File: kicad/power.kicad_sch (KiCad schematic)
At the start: 27 parts, among them U3 MIMXRT1171DVMAB, Y3 24MHz, Y4 32.768kHz

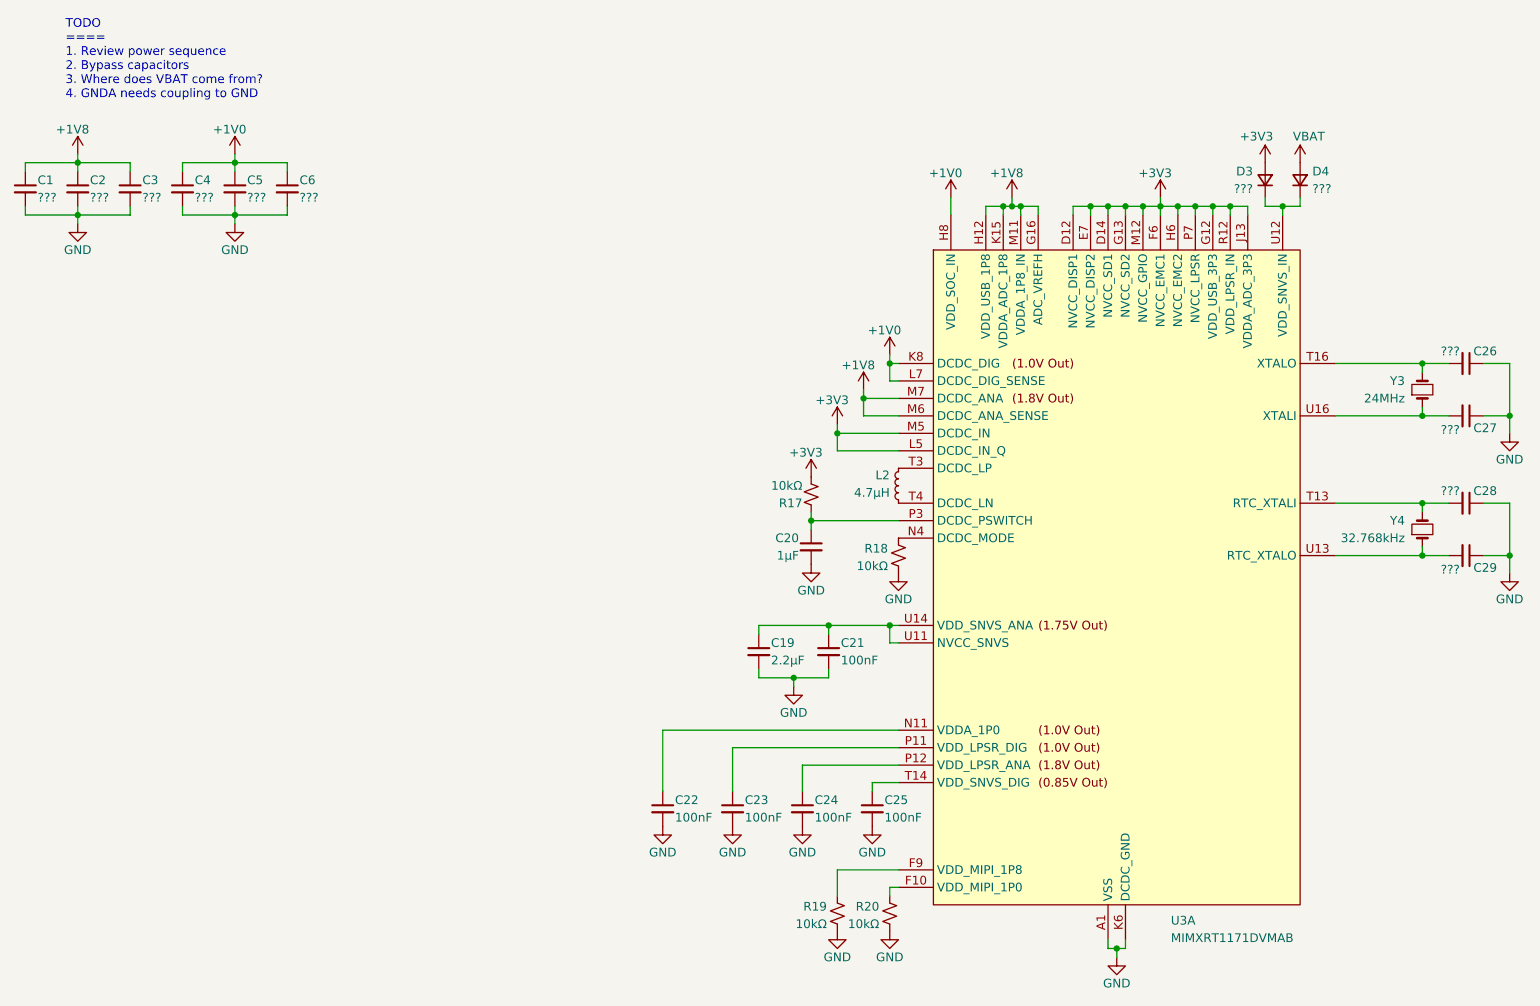
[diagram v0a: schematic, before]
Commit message: reworked design to use 1.8V logic
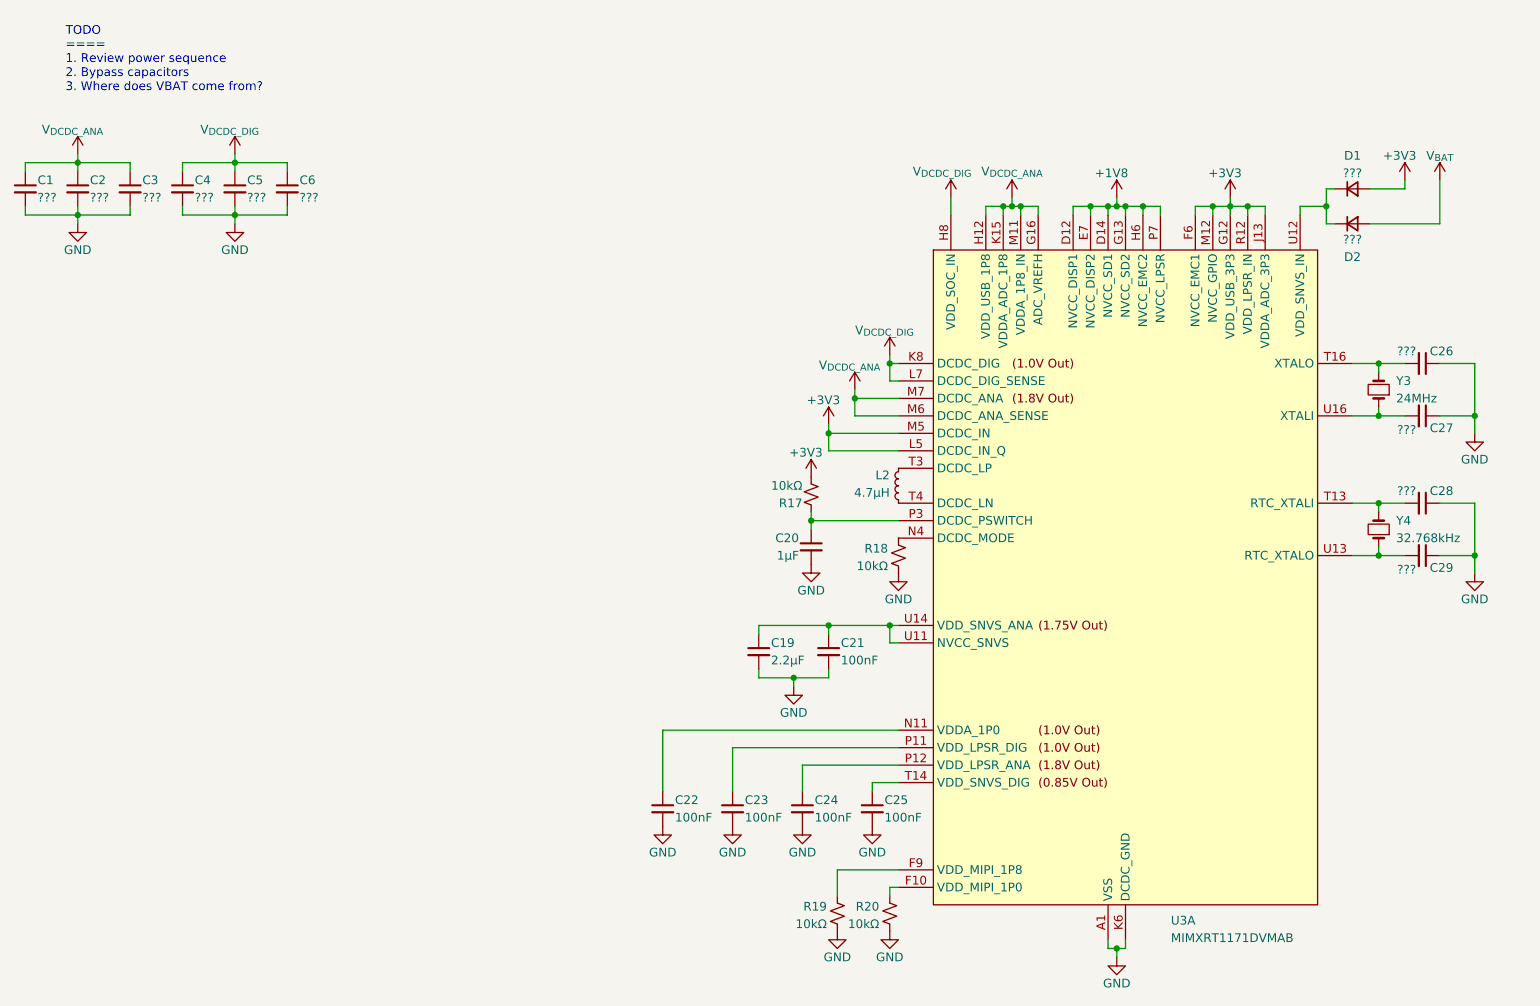
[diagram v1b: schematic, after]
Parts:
- removed D3, D4: ???, symbol Device:D_Small
- added D1, D2: ???, symbol Device:D_Small
- U3: footprint (none) -> Package_BGA:MAPBGA-289_14x14mm_Layout17x17_P0.8mm
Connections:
- net +1V8: now also U3.D12 (NVCC_DISP1), U3.D14 (NVCC_SD1), U3.E7 (NVCC_DISP2), U3.G13 (NVCC_SD2), U3.H6 (NVCC_EMC2), U3.J6 (NVCC_EMC2), U3.P7 (NVCC_LPSR); no longer C1.1, C2.1, C3.1, U3.G16 (ADC_VREFH), U3.H12 (VDD_USB_1P8), U3.K15 (VDDA_ADC_1P8), U3.M11 (VDDA_1P8_IN), U3.M6 (DCDC_ANA_SENSE), U3.M7 (DCDC_ANA), U3.M8 (DCDC_ANA)
- net +3V3: now also D1.2 (A); no longer U3.D12 (NVCC_DISP1), U3.D14 (NVCC_SD1), U3.E7 (NVCC_DISP2), U3.G13 (NVCC_SD2), U3.H6 (NVCC_EMC2), U3.J6 (NVCC_EMC2), U3.P7 (NVCC_LPSR)
- net at U3.U12 (VDD_SNVS_IN): now also D1.1 (K), D2.1 (K)
- net +1V0 renamed V_{DCDC_DIG}
- new net V_{BAT}: D2.2 (A)
- new net V_{DCDC_ANA}: C1.1, C2.1, C3.1, U3.G16 (ADC_VREFH), U3.H12 (VDD_USB_1P8), U3.K15 (VDDA_ADC_1P8), U3.M11 (VDDA_1P8_IN), U3.M6 (DCDC_ANA_SENSE), U3.M7 (DCDC_ANA), U3.M8 (DCDC_ANA)
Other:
- note added: "TODO ==== 1. Review power sequence 2. Bypass capacitors 3. Where does VBAT come from?"
- note removed: "TODO ==== 1. Review power sequence 2. Bypass capacitors 3. Where does VBAT come from? 4. GNDA needs coupling to GND"
- moved on the sheet: U3A

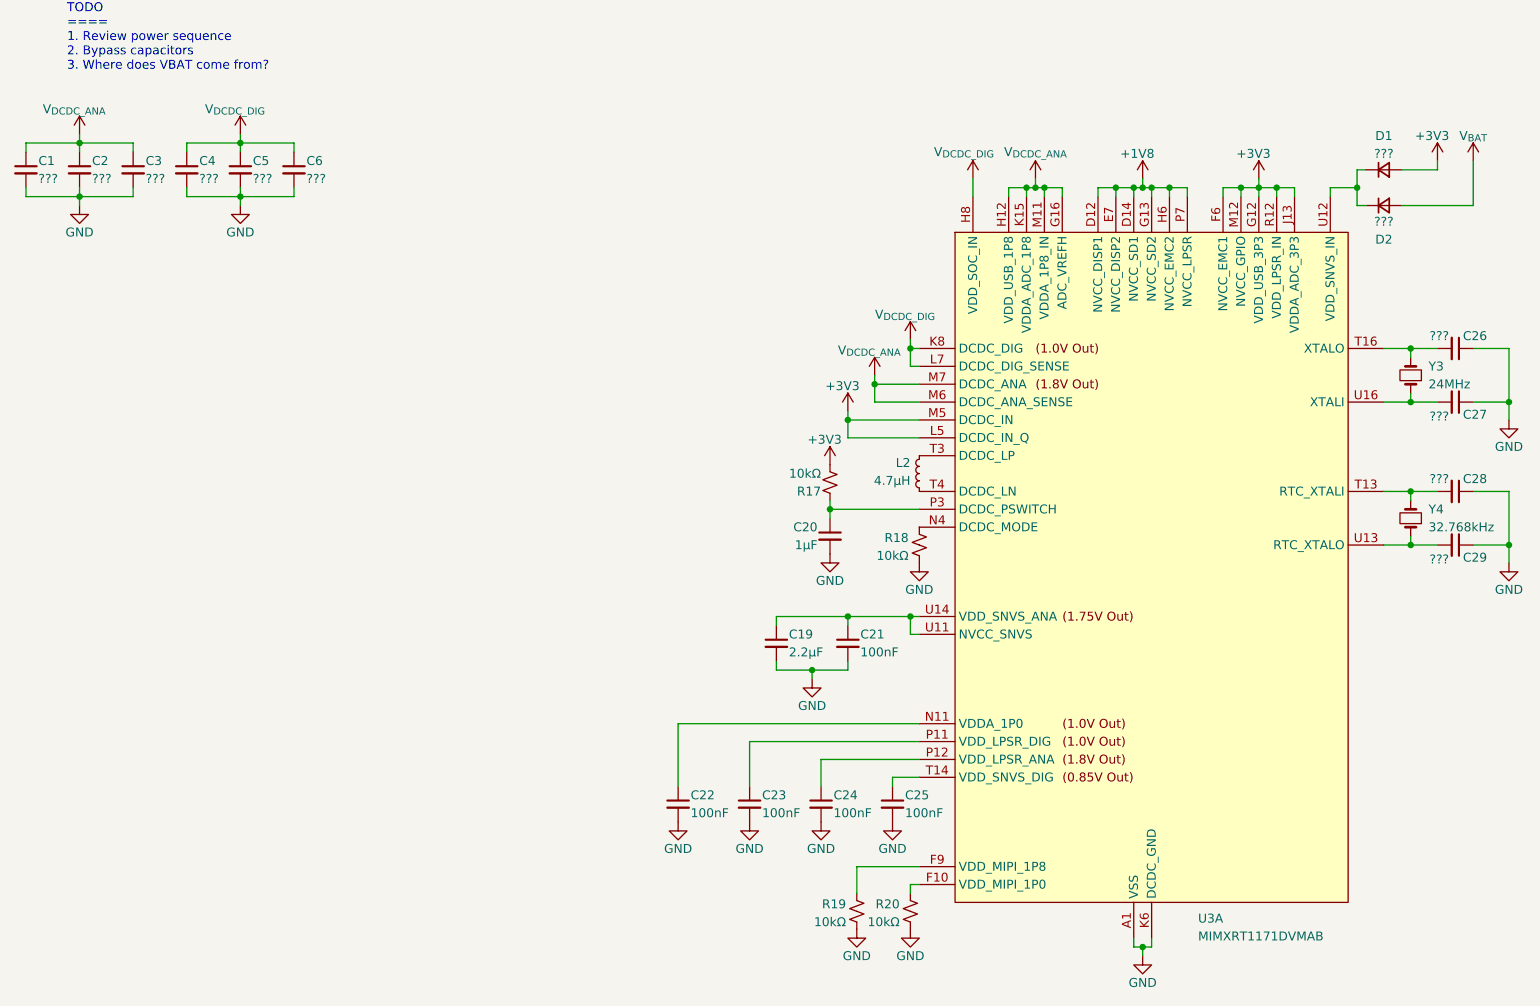
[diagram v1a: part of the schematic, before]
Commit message: added user button and LED
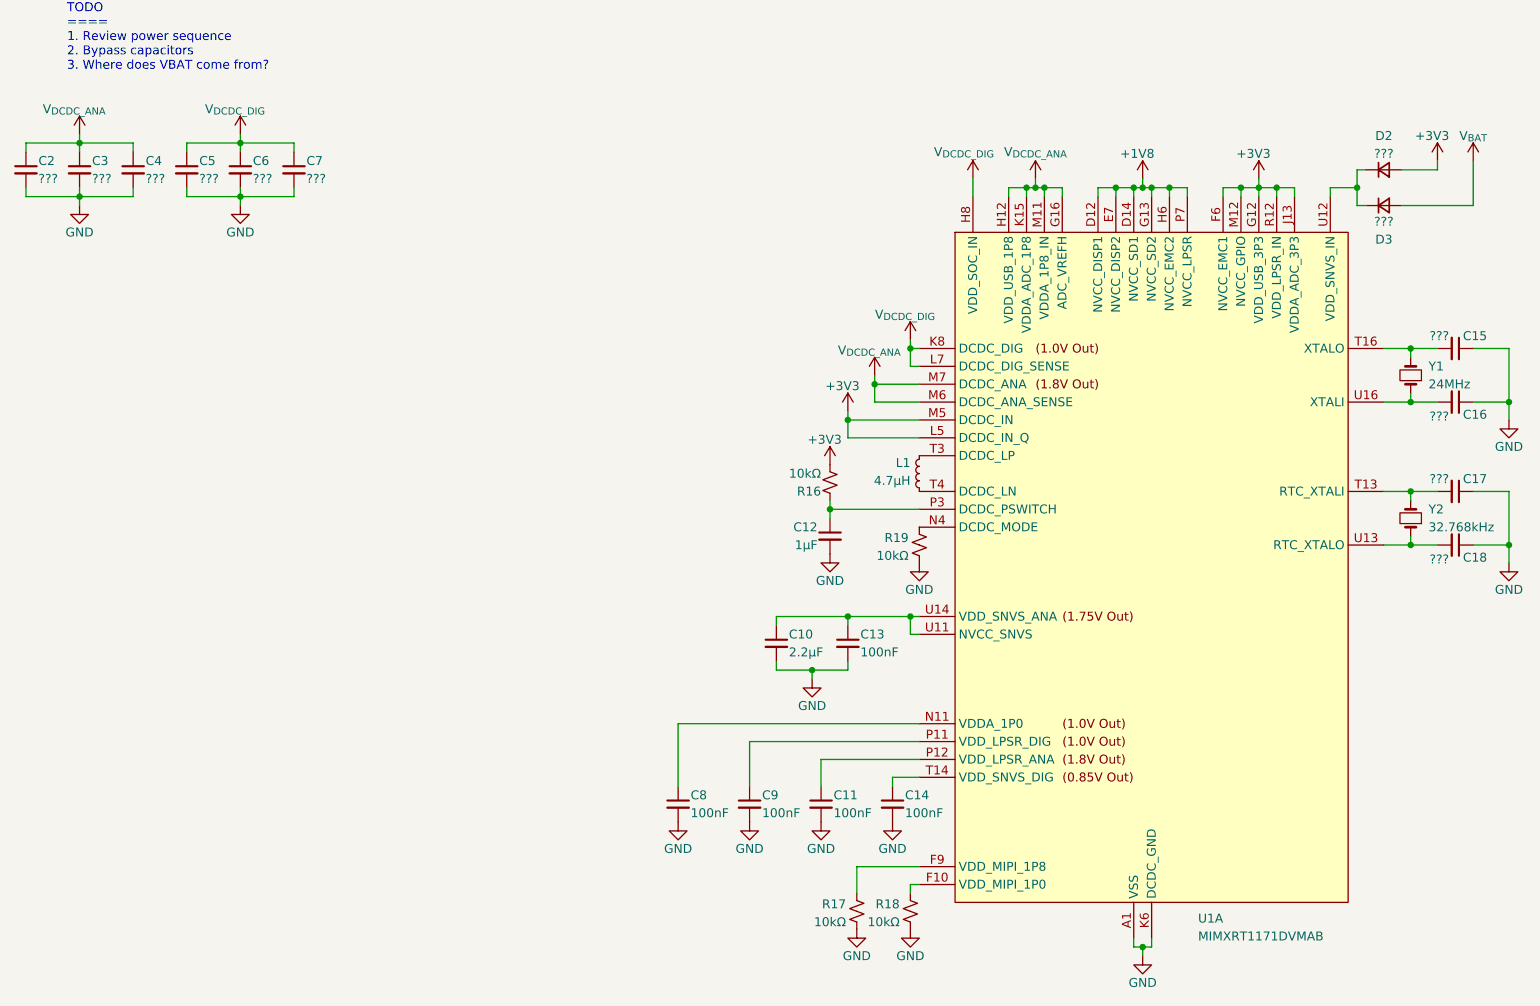
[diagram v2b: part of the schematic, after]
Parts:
- renumbered C19 to C10, C24 to C11, C20 to C12, C21 to C13, C25 to C14, C26 to C15, C27 to C16, C28 to C17, C29 to C18, C1 to C2, C2 to C3, C3 to C4, C4 to C5, C5 to C6, C6 to C7, C22 to C8, C23 to C9, D1 to D2, D2 to D3, L2 to L1, R17 to R16, R19 to R17, R20 to R18, R18 to R19, U3 to U1, Y3 to Y1, Y4 to Y2

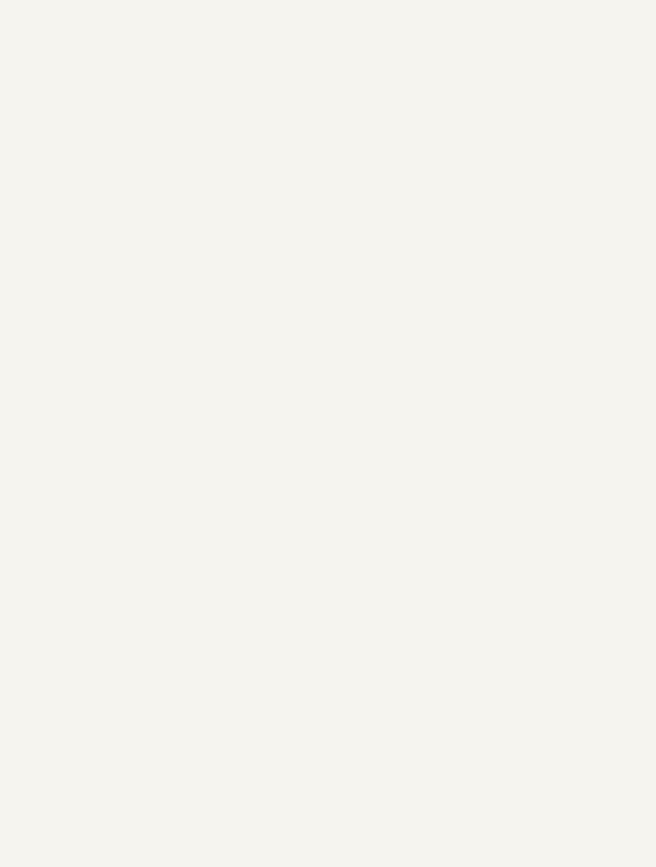
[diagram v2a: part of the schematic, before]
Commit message: added 3.3V and 1.8V buck converters to schematic
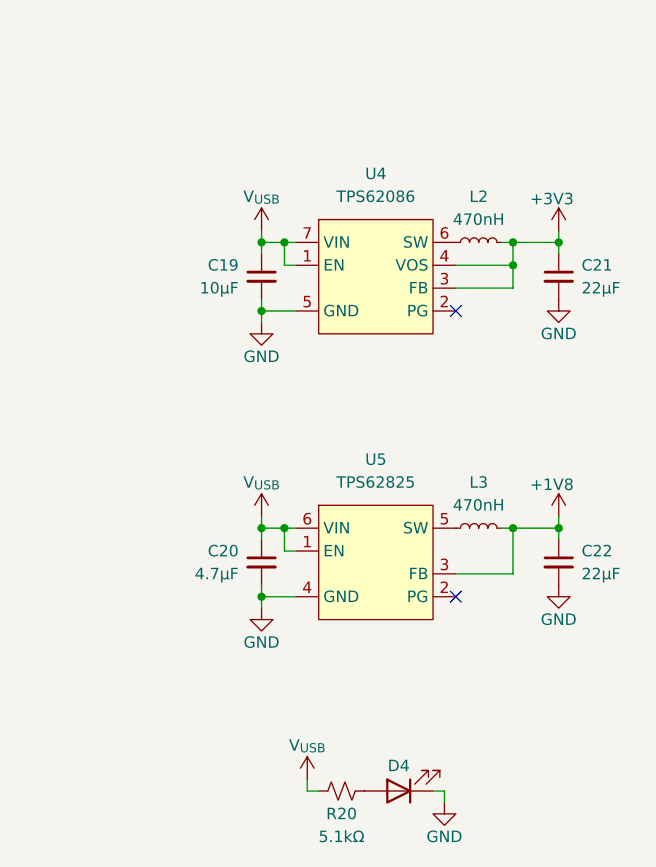
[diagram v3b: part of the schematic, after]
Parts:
- added C19: 10μF, symbol Device:C_Small
- added C20: 4.7μF, symbol Device:C_Small
- added C21, C22: 22μF, symbol Device:C_Small
- added D4: RED, symbol Device:LED
- added L2, L3: 470nH, symbol Device:L_Small
- added R20: 5.1kΩ, symbol Device:R_Small_US
- added U4: TPS62086, symbol project_symbols:TPS62086
- added U5: TPS62825, symbol project_symbols:TPS62825
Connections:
- net +1V8: now also C22.1, L3.2, U5.3 (FB)
- net +3V3: now also C21.1, L2.2, U4.3 (FB), U4.4 (VOS)
- net GND: now also C19.2, C20.2, C21.2, C22.2, D4.1 (K), U4.5 (GND), U5.4 (GND)
- new net: L3.1, U5.5 (SW)
- new net: L2.1, U4.6 (SW)
- new net: D4.2 (A), R20.2
- new net V_{USB}: C19.1, C20.1, R20.1, U4.1 (EN), U4.7 (VIN), U5.1 (EN), U5.6 (VIN)
- no-connect marks 0 -> 2

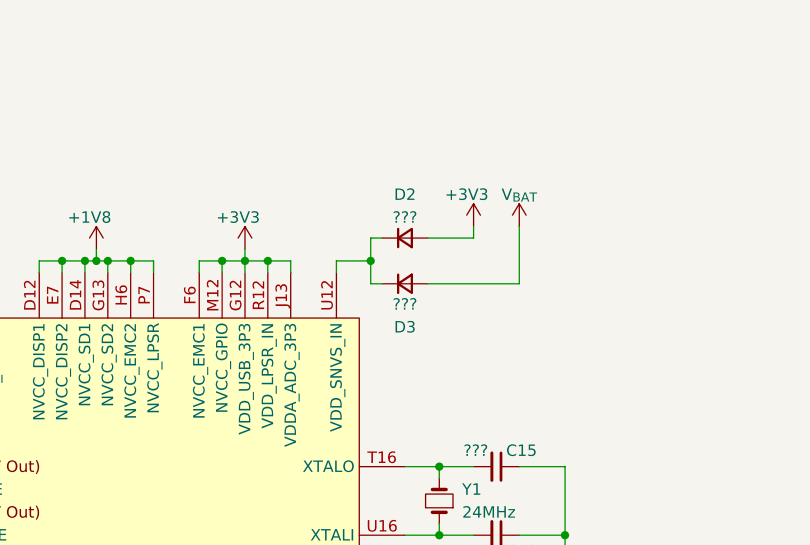
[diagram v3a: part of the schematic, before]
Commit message: added IMU to schematic
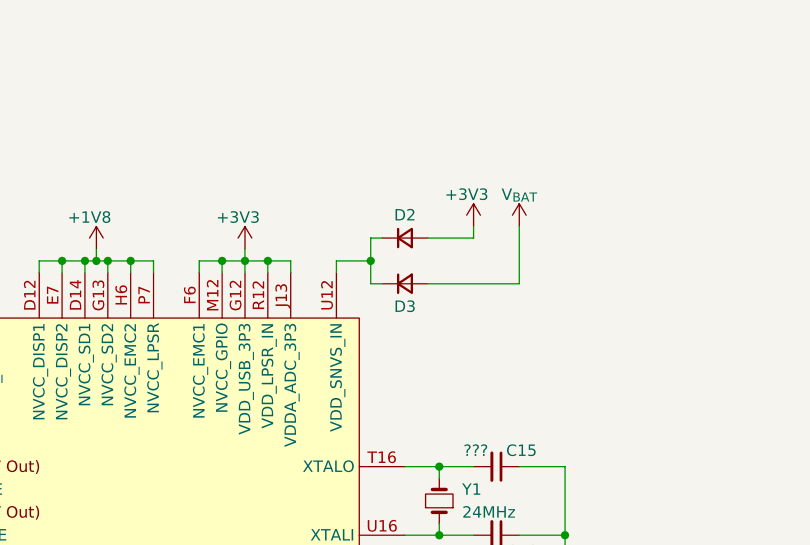
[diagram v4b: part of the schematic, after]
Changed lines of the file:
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@@
 		(dnp no)
 		(property "Reference" "D3"
-			(at 138.43 49.276 0)
+			(at 138.43 46.99 0)
 			(show_name no)
 			(do_not_autoplace no)
@@
 		(property "Value" "???"
 			(at 138.43 46.736 0)
+			(hide yes)
 			(show_name no)
 			(do_not_autoplace no)
@@
 		(dnp no)
 		(property "Reference" "D2"
-			(at 138.43 34.544 0)
+			(at 138.43 36.83 0)
 			(show_name no)
 			(do_not_autoplace no)
@@
 		(property "Value" "???"
 			(at 138.43 37.084 0)
+			(hide yes)
 			(show_name no)
 			(do_not_autoplace no)
